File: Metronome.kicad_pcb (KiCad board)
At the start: 2 copper layers, 25.3 x 25.1 mm, 30 parts, among them CON1 PDI_50mil, IC1 ATXMEGA8E5-MU, P1 USB_B, Q1 Q_PMOS_GSD, U1 AS1117, U2 NCP706A

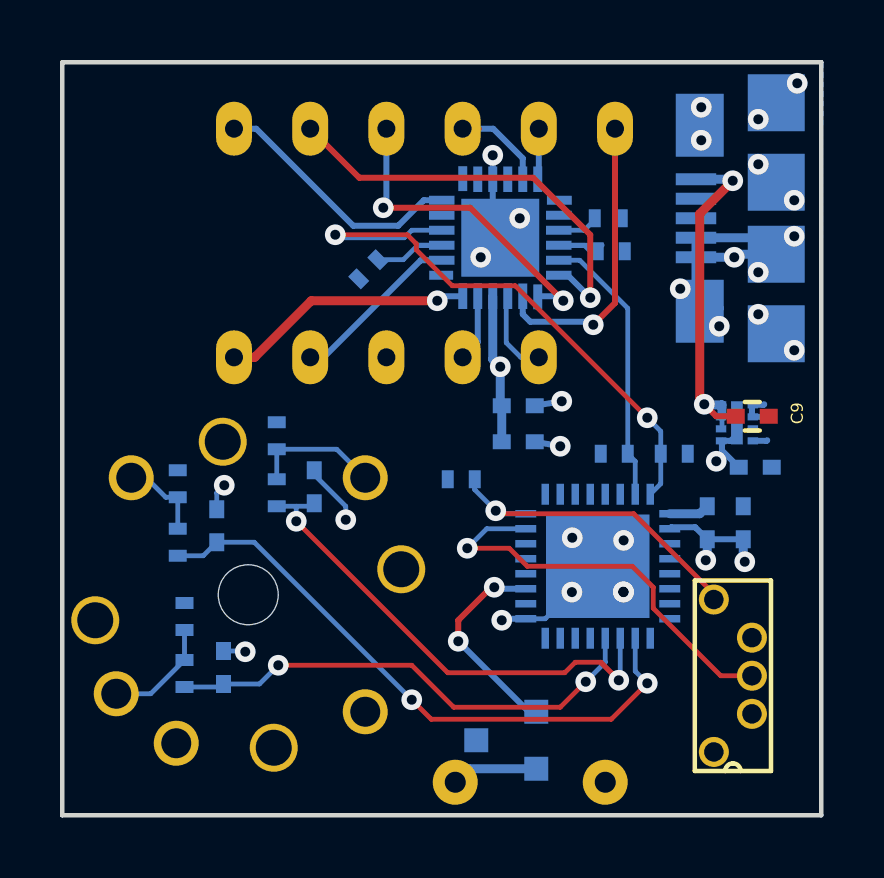
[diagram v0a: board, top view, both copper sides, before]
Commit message: Optimize layout to fit buzzer on board. Add ID pin to USB micro B connector.
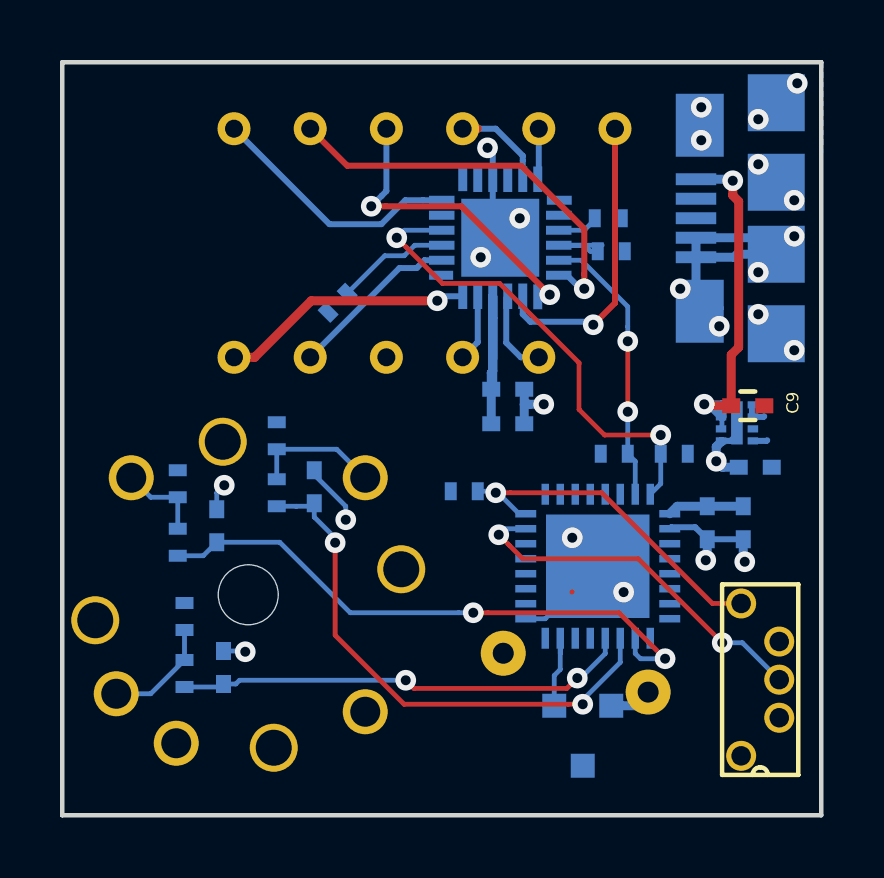
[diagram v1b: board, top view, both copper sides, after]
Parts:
- R10, R11, R12: value 40k -> 41.2k
- R8, R9: value 20k -> 21k
- moved SP1 3.95 mm to (84.4, 88.1), turned to 165 degrees
- moved Q1 2.55 mm to (84.7, 90.2), turned to 0 degrees
- moved R10 1.51 mm to (76.5, 75.8)
- moved CON1 0.92 mm to (88.7, 88.4)
- moved C7 0.69 mm to (82.2, 79.8)
- moved C6 0.65 mm to (82.2, 78.7)
- moved R1 0.41 mm to (80.7, 82.1)
- moved C9 0.38 mm to (90.2, 79.2)
- turned R3 to 270 degrees
- turned R5 to 270 degrees
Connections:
- P1 pad 6: (no net) -> GND
- Q1 pad 1: Net-(IC1-Pad3) -> Net-(IC1-Pad31)
- R3 pad 1: Net-(R2-Pad1) -> VCC
- R3 pad 2: VCC -> Net-(R2-Pad1)
- R5 pad 1: Net-(R4-Pad1) -> VCC
- R5 pad 2: VCC -> Net-(R4-Pad1)
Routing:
- net Net-(IC1-Pad3): track 7.00 -> 0.00 mm, vias 2 -> 0
- net VCC: track 8.44 -> 13.8 mm, vias 1 -> 0
- net GND: track 37.3 -> 42.6 mm, vias 22 -> 24
- net (no net): track 3.72 -> 0.02 mm, vias 8 -> 0
- net Net-(IC1-Pad16): track 19.6 -> 16.3 mm
- net Net-(IC1-Pad31): track 0.00 -> 2.84 mm
- net Net-(CON1-Pad3): track 14.3 -> 12.3 mm, vias 1 -> 2
- net /ROTA: track 16.3 -> 15.2 mm
- net Net-(Q1-Pad2): track 2.89 -> 2.06 mm
- net Net-(CON1-Pad6): track 11.0 -> 11.8 mm
- net Net-(7Seg1-Pad11): track 14.3 -> 13.6 mm
- net Net-(R10-Pad1): track 3.13 -> 3.81 mm
- net /SW1: track 20.4 -> 19.8 mm
- net /ROTB: track 17.3 -> 17.9 mm
- net Net-(R2-Pad1): track 2.87 -> 3.37 mm
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
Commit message: Not sure.
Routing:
- net /ROTB: track 17.9 -> 16.5 mm, vias 2 -> 4
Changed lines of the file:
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@@
-(kicad_pcb (version 4) (host pcbnew "(2015-10-28 BZR 6285, Git 77f1d8a)-product")
+(kicad_pcb (version 4) (host pcbnew "(2015-10-27 BZR 6284)-product")
   (general
     (links 92)
-    (no_connects 4)
+    (no_connects 0)
     (area 67.224999 67.724999 92.675001 92.975001)
     (thickness 1.6)
     (drawings 6)
-    (tracks 306)
+    (tracks 313)
     (zones 0)
     (modules 30)
@@
   (segment (start 81.65 71.7) (end 81.65 72.6) (width 0.2) (layer B.Cu) (net 2) (status 30))
   (segment (start 81.65 72.6) (end 81.25 73) (width 0.2) (layer B.Cu) (net 2) (status 30))
-  (segment (start 84.122426 88.67261) (end 79.02261 88.67261) (width 0.16) (layer F.Cu) (net 3))
-  (segment (start 79.02261 88.67261) (end 78.75 88.4) (width 0.16) (layer F.Cu) (net 3))
-  (segment (start 84.467425 88.327611) (end 84.122426 88.67261) (width 0.16) (layer F.Cu) (net 3))
+  (segment (start 85.06 87.85) (end 84.6 87.85) (width 0.16) (layer B.Cu) (net 3))
+  (segment (start 85.4 87.51) (end 85.06 87.85) (width 0.16) (layer B.Cu) (net 3))
+  (segment (start 85.4 87) (end 85.4 87.51) (width 0.16) (layer B.Cu) (net 3))
+  (segment (start 84.255001 88.194999) (end 84.6 87.85) (width 0.16) (layer F.Cu) (net 3))
+  (via (at 84.6 87.85) (size 0.69) (drill 0.331) (layers F.Cu B.Cu) (net 3))
+  (segment (start 78.75 88.4) (end 79.094999 88.744999) (width 0.16) (layer F.Cu) (net 3))
+  (segment (start 79.094999 88.744999) (end 83.705001 88.744999) (width 0.16) (layer F.Cu) (net 3))
+  (segment (start 83.705001 88.744999) (end 84.255001 88.194999) (width 0.16) (layer F.Cu) (net 3))
   (segment (start 73.21 88.4) (end 78.75 88.4) (width 0.16) (layer B.Cu) (net 3))
   (segment (start 73.085 88.525) (end 73.21 88.4) (width 0.16) (layer B.Cu) (net 3))
   (segment (start 72.675 88.525) (end 73.085 88.525) (width 0.16) (layer B.Cu) (net 3))
   (via (at 78.75 88.4) (size 0.69) (drill 0.331) (layers F.Cu B.Cu) (net 3))
-  (segment (start 84.582389 88.327611) (end 84.467425 88.327611) (width 0.16) (layer B.Cu) (net 3))
-  (segment (start 85.4 87.51) (end 84.582389 88.327611) (width 0.16) (layer B.Cu) (net 3))
-  (segment (start 85.4 87) (end 85.4 87.51) (width 0.16) (layer B.Cu) (net 3))
-  (via (at 84.467425 88.327611) (size 0.69) (drill 0.331) (layers F.Cu B.Cu) (net 3))
   (segment (start 71.375 88.625) (end 72.575 88.625) (width 0.16) (layer B.Cu) (net 3) (status 30))
   (segment (start 72.575 88.625) (end 72.675 88.525) (width 0.16) (layer B.Cu) (net 3) (status 30))
@@
   (segment (start 90.29 79.62) (end 90.29 79.22) (width 0.2) (layer B.Cu) (net 4))
   (segment (start 81.65 75.6) (end 81.65 77.7) (width 0.3) (layer B.Cu) (net 4) (status 10))
-  (segment (start 76.396985 86.901539) (end 78.69545 89.200004) (width 0.16) (layer F.Cu) (net 5))
-  (segment (start 84.162097 89.200004) (end 84.65 89.200004) (width 0.16) (layer F.Cu) (net 5))
-  (segment (start 76.396985 83.814866) (end 76.396985 86.901539) (width 0.16) (layer F.Cu) (net 5))
-  (segment (start 78.69545 89.200004) (end 84.162097 89.200004) (width 0.16) (layer F.Cu) (net 5))
+  (segment (start 81.55 89.35) (end 81.912101 89.35) (width 0.16) (layer B.Cu) (net 5))
+  (segment (start 79.95 87.75) (end 81.55 89.35) (width 0.16) (layer B.Cu) (net 5))
+  (segment (start 81.912101 89.35) (end 82.400004 89.35) (width 0.16) (layer B.Cu) (net 5))
+  (segment (start 82.55 89.200004) (end 82.400004 89.35) (width 0.16) (layer F.Cu) (net 5))
+  (segment (start 84.65 89.200004) (end 82.55 89.200004) (width 0.16) (layer F.Cu) (net 5))
+  (via (at 82.400004 89.35) (size 0.69) (drill 0.331) (layers F.Cu B.Cu) (net 5))
+  (segment (start 76.396985 83.814866) (end 76.396985 84.302769) (width 0.16) (layer F.Cu) (net 5))
+  (segment (start 76.396985 84.302769) (end 79.844216 87.75) (width 0.16) (layer F.Cu) (net 5))
+  (segment (start 79.844216 87.75) (end 79.95 87.75) (width 0.16) (layer F.Cu) (net 5))
+  (via (at 79.95 87.75) (size 0.69) (drill 0.331) (layers F.Cu B.Cu) (net 5))
   (segment (start 85.9 87.804554) (end 84.65 89.054554) (width 0.16) (layer B.Cu) (net 5))
   (via (at 84.65 89.200004) (size 0.69) (drill 0.331) (layers F.Cu B.Cu) (net 5))
@@
   (segment (start 87.25 80.85) (end 87.25 81.85) (width 0.16) (layer B.Cu) (net 18) (status 10))
   (segment (start 87.25 81.85) (end 86.9 82.2) (width 0.16) (layer B.Cu) (net 18) (status 20))
-  (segment (start 83.7 88.24048) (end 83.7 88.68919) (width 0.16) (layer B.Cu) (net 28))
+  (segment (start 83.7 87.995446) (end 83.7 88.68919) (width 0.16) (layer B.Cu) (net 28))
+  (segment (start 83.9 87) (end 83.9 87.795446) (width 0.16) (layer B.Cu) (net 28))
+  (segment (start 83.9 87.795446) (end 83.7 87.995446) (width 0.16) (layer B.Cu) (net 28))
   (segment (start 83.7 88.68919) (end 83.7 89.24924) (width 0.16) (layer B.Cu) (net 28))
-  (segment (start 83.9 88.04048) (end 83.7 88.24048) (width 0.16) (layer B.Cu) (net 28))
-  (segment (start 83.9 87) (end 83.9 88.04048) (width 0.16) (layer B.Cu) (net 28))
   (segment (start 83.9 87.51) (end 83.9 87) (width 0.16) (layer B.Cu) (net 28))
   (segment (start 71.15 82.3) (end 70.25 82.3) (width 0.16) (layer B.Cu) (net 29))

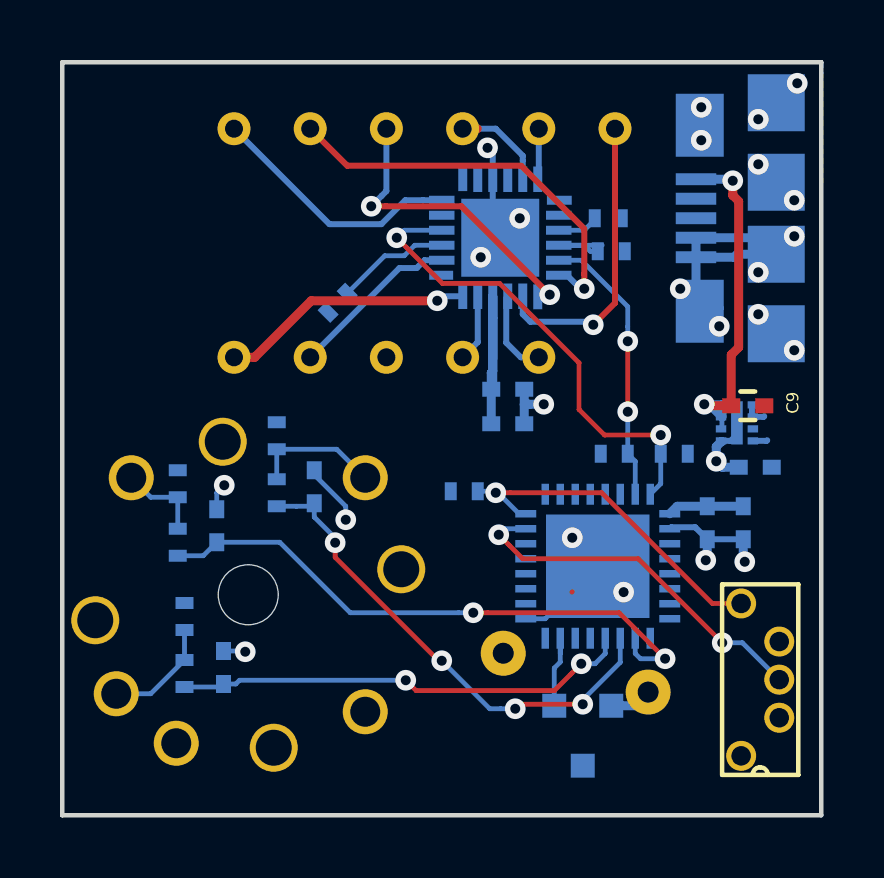
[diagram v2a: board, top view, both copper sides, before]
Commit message: Add 32kHz crystal to XMega circuit.
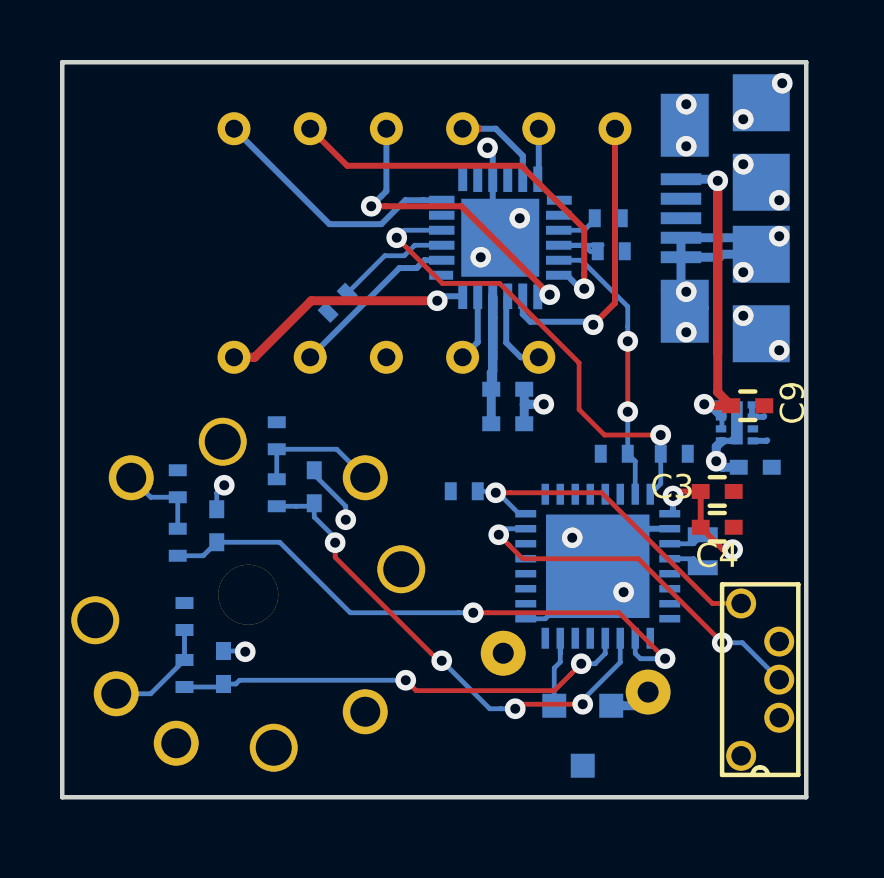
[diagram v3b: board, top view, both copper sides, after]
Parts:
- added Y1: Crystal, crystal_ABS05_Abracon_smd, B.Cu at (88.7, 84.1)
- C3, C4: moved to F.Cu
- S1: footprint EC09E15244xx -> footprints:EC09E15244xx
- moved C3 1.09 mm to (89.1, 82.1), turned to 0 degrees
- moved C4 0.88 mm to (89.1, 83.3), turned to 0 degrees
- moved P1 0.50 mm to (90.6, 73.0)
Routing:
- net Net-(C9-Pad1): track 12.0 -> 17.8 mm
- net VCC: track 13.8 -> 16.1 mm, vias 0 -> 2
- net Net-(IC1-Pad20): track 0.00 -> 1.22 mm
- net Net-(IC1-Pad19): track 0.00 -> 1.22 mm
- net GND: track 42.6 -> 41.9 mm, vias 24 -> 22
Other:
- board size 25.3 x 25.1 mm -> 24.8 x 24.5 mm
- board text added: "Micronome Rev. 1.0 © Kevin Ward 2015"
